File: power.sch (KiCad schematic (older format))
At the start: 56 parts, among them J4 Conn_01x02, J5 Conn_01x02, J6 Conn_01x02, Q29 AO3401, Q30 Q_NPN_BEC, T1 COMMON_MODE_CHOKE, U14 AP1117-33, U19 TPS54428DDA, U2 TPS54202

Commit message: Specified 3V3 LDO as ON semi NCP1117 because its document shows stable MLCC output capacitor capcity/ESR range
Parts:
- U14: value AP1117-33 -> NCP1117ST33
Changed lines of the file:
@@
 P 4950 3600
 F 0 "U14" H 4950 3842 50  0000 C CNN
-F 1 "AP1117-33" H 4950 3751 50  0000 C CNN
+F 1 "NCP1117ST33" H 4950 3751 50  0000 C CNN
 F 2 "Package_TO_SOT_SMD:SOT-223-3_TabPin2" H 4950 3800 50  0001 C CNN
 F 3 "http://www.diodes.com/datasheets/AP1117.pdf" H 5050 3350 50  0001 C CNN

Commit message: Changed HC595's vdd from LEDVDD to LEDLOGICVDD; Fixed silk refdes'; DRC clean ?(unchecked)
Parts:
- added C79: 1u/35V, Capacitor_SMD:C_0603_1608Metric_Pad1.05x0.95mm_HandSolder, symbol dotmatrix_64x48-rescue:C-device
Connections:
- wire segments 137 -> 138
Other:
- note added: "Note that:\nRow driver's P-MOSFET gate voltage swings between\nLEDLOGICVDD(off-state) and GND(on-state),\nso LEDVDD cannot be high over that point that LEDLOGICVDD\nbecomes below threshold gate voltage of the P-MOSFET.\n\n"
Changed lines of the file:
@@
 AR Path="/5BB82B1A" Ref="C?"  Part="1"
 AR Path="/59A82F84/5BB82B1A" Ref="C65"  Part="1"
-F 0 "C65" H 8050 3800 50  0000 L CNN
-F 1 "0.1u/35V" H 8050 3700 50  0000 L CNN
+F 0 "C65" H 8450 3400 50  0000 L CNN
+F 1 "0.1u/35V" H 8350 3300 50  0000 L CNN
 F 2 "Capacitor_SMD:C_0603_1608Metric_Pad1.05x0.95mm_HandSolder" H 8365 3809 50  0001 L CNN
 F 3 "" H 8250 3900 50  0000 C CNN
@@
 AR Path="/5BB82B13" Ref="C?"  Part="1"
 AR Path="/59A82F84/5BB82B13" Ref="C62"  Part="1"
-F 0 "C62" H 7850 3800 50  0000 L CNN
-F 1 "1u/35V" H 7900 3700 50  0000 L CNN
+F 0 "C62" H 7950 3400 50  0000 L CNN
+F 1 "1u/35V" H 7850 3300 50  0000 L CNN
 F 2 "Capacitor_SMD:C_0603_1608Metric_Pad1.05x0.95mm_HandSolder" H 8115 3809 50  0001 L CNN
 F 3 "" H 8000 3900 50  0000 C CNN
@@
 Connection ~ 6000 3100
 Wire Wire Line
-	6000 3100 6850 3100
+	6000 3100 6450 3100
 Wire Wire Line
 	4200 5400 4250 5400
@@
 	0    1    1    0
 $EndComp
+Text Notes 5850 5650 0    50   ~ 0
+Note that:\nRow driver's P-MOSFET gate voltage swings between\nLEDLOGICVDD(off-state) and GND(on-state),\nso LEDVDD cannot be high over that point that LEDLOGICVDD\nbecomes below threshold gate voltage of the P-MOSFET.\n\n
+$Comp
+L dotmatrix_64x48-rescue:C-device C?
+U 1 1 5DDD7208
+P 6450 3250
+AR Path="/59A8E319/5DDD7208" Ref="C?"  Part="1"
+AR Path="/5DDD7208" Ref="C?"  Part="1"
+AR Path="/59A82F84/5DDD7208" Ref="C79"  Part="1"
+F 0 "C79" H 6400 2750 50  0000 L CNN
+F 1 "1u/35V" H 6300 2650 50  0000 L CNN
+F 2 "Capacitor_SMD:C_0603_1608Metric_Pad1.05x0.95mm_HandSolder" H 6565 3159 50  0001 L CNN
+F 3 "" H 6450 3250 50  0000 C CNN
+	1    6450 3250
+	1    0    0    -1
+$EndComp
+Connection ~ 6450 3100
+Wire Wire Line
+	6450 3100 6850 3100
+$Comp
+L dotmatrix_64x48-rescue:GND-power #PWR?
+U 1 1 5DDD7589
+P 6450 3400
+AR Path="/59A8E319/5DDD7589" Ref="#PWR?"  Part="1"
+AR Path="/5DDD7589" Ref="#PWR?"  Part="1"
+AR Path="/59A82F84/5DDD7589" Ref="#PWR014"  Part="1"
+F 0 "#PWR014" H 6450 3150 50  0001 C CNN
+F 1 "GND" H 6450 3250 50  0000 C CNN
+F 2 "" H 6450 3400 50  0000 C CNN
+F 3 "" H 6450 3400 50  0000 C CNN
+	1    6450 3400
+	-1   0    0    -1
+$EndComp
 $EndSCHEMATC

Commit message: Fixed USB micro-b's mount polarity; Improved SOT-23-6 1-pin silk marker readability
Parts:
- U2: footprint TO_SOT_Packages_SMD:SOT-23-6 -> components:SOT-23-6_Handsoldering_mod
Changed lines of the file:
@@
 F 0 "U2" H 2000 3867 50  0000 C CNN
 F 1 "TPS54202" H 2000 3776 50  0000 C CNN
-F 2 "TO_SOT_Packages_SMD:SOT-23-6" H 2000 2900 50  0001 C CIN
+F 2 "components:SOT-23-6_Handsoldering_mod" H 2000 2900 50  0001 C CIN
 F 3 "http://www.ti.com/lit/ds/symlink/tps54202.pdf" H 1600 3850 50  0001 C CNN
 	1    2000 3400

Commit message: LEDVDD now can be up to 5.0V for blue/white LEDs; DRC clear
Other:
- note added: "LEDVDD must be from min 3.1V to max 5.0V"
- note removed: "Note that:\nRow driver's P-MOSFET gate voltage swings between\nLEDLOGICVDD(off-state) and GND(on-state),\nso LEDVDD cannot be high over that point that LEDLOGICVDD\nbecomes below threshold gate voltage of the P-MOSFET.\n\n"
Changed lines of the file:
@@
 $EndComp
 Text Notes 5850 5650 0    50   ~ 0
-Note that:\nRow driver's P-MOSFET gate voltage swings between\nLEDLOGICVDD(off-state) and GND(on-state),\nso LEDVDD cannot be high over that point that LEDLOGICVDD\nbecomes below threshold gate voltage of the P-MOSFET.\n\n
+LEDVDD  must be from min 3.1V to max 5.0V
 $Comp
 L dotmatrix_64x48-rescue:C-device C?

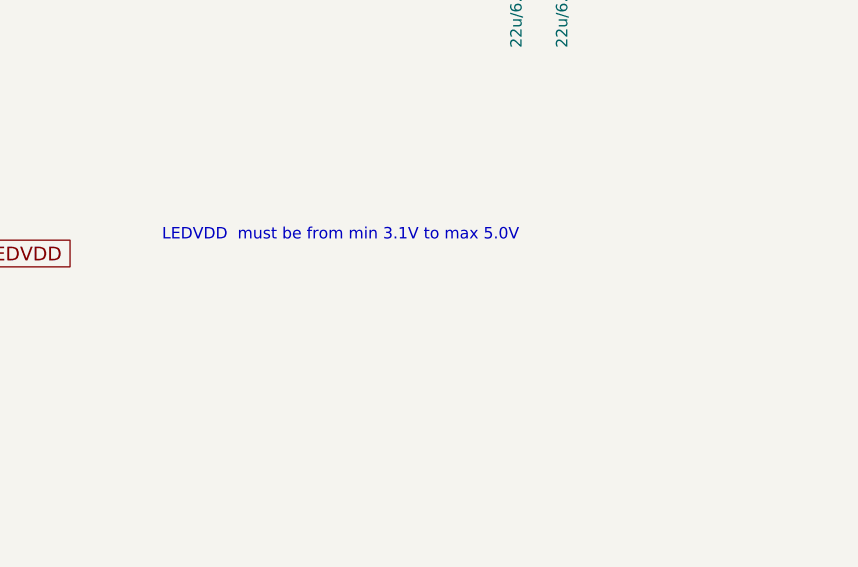
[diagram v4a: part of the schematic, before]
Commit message: Wrote note about making LEDVDD > 4.5V
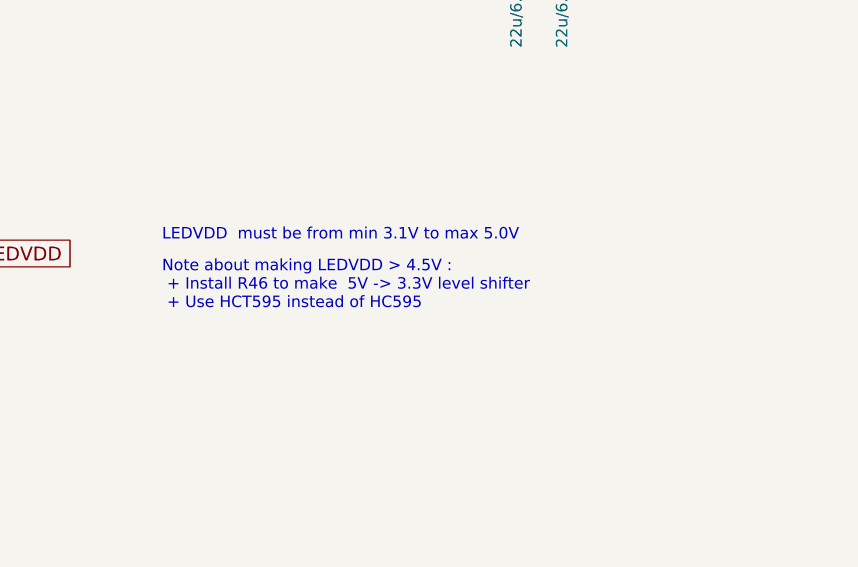
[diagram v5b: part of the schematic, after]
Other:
- note added: "Note about making LEDVDD > 4.5V :\n + Install R46 to make 5V -> 3.3V level shifter\n + Use HCT595 instead of HC595\n"
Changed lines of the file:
@@
 	-1   0    0    -1
 $EndComp
+Text Notes 5850 5950 0    50   ~ 0
+Note about making LEDVDD > 4.5V :\n + Install R46 to make  5V -> 3.3V level shifter\n + Use HCT595 instead of HC595\n
 $EndSCHEMATC

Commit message: Improved thermal dissipation around DC-DC converters
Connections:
- wire segments 138 -> 152
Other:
- note added: "AGND"
- note added: "PGND"

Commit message: Schematics format change due to KiCAD's verup
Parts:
- D7, D9: value 14V TVS diode -> 16V TVS diode
